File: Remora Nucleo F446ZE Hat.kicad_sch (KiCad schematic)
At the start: 12 parts, among them J1 NucleoF446RE CN10 Header, J11 UART OUT, J17 5V_AUXOUT, J2 NucleoF446RE CN7 Header, J4 5V_SUPPLY

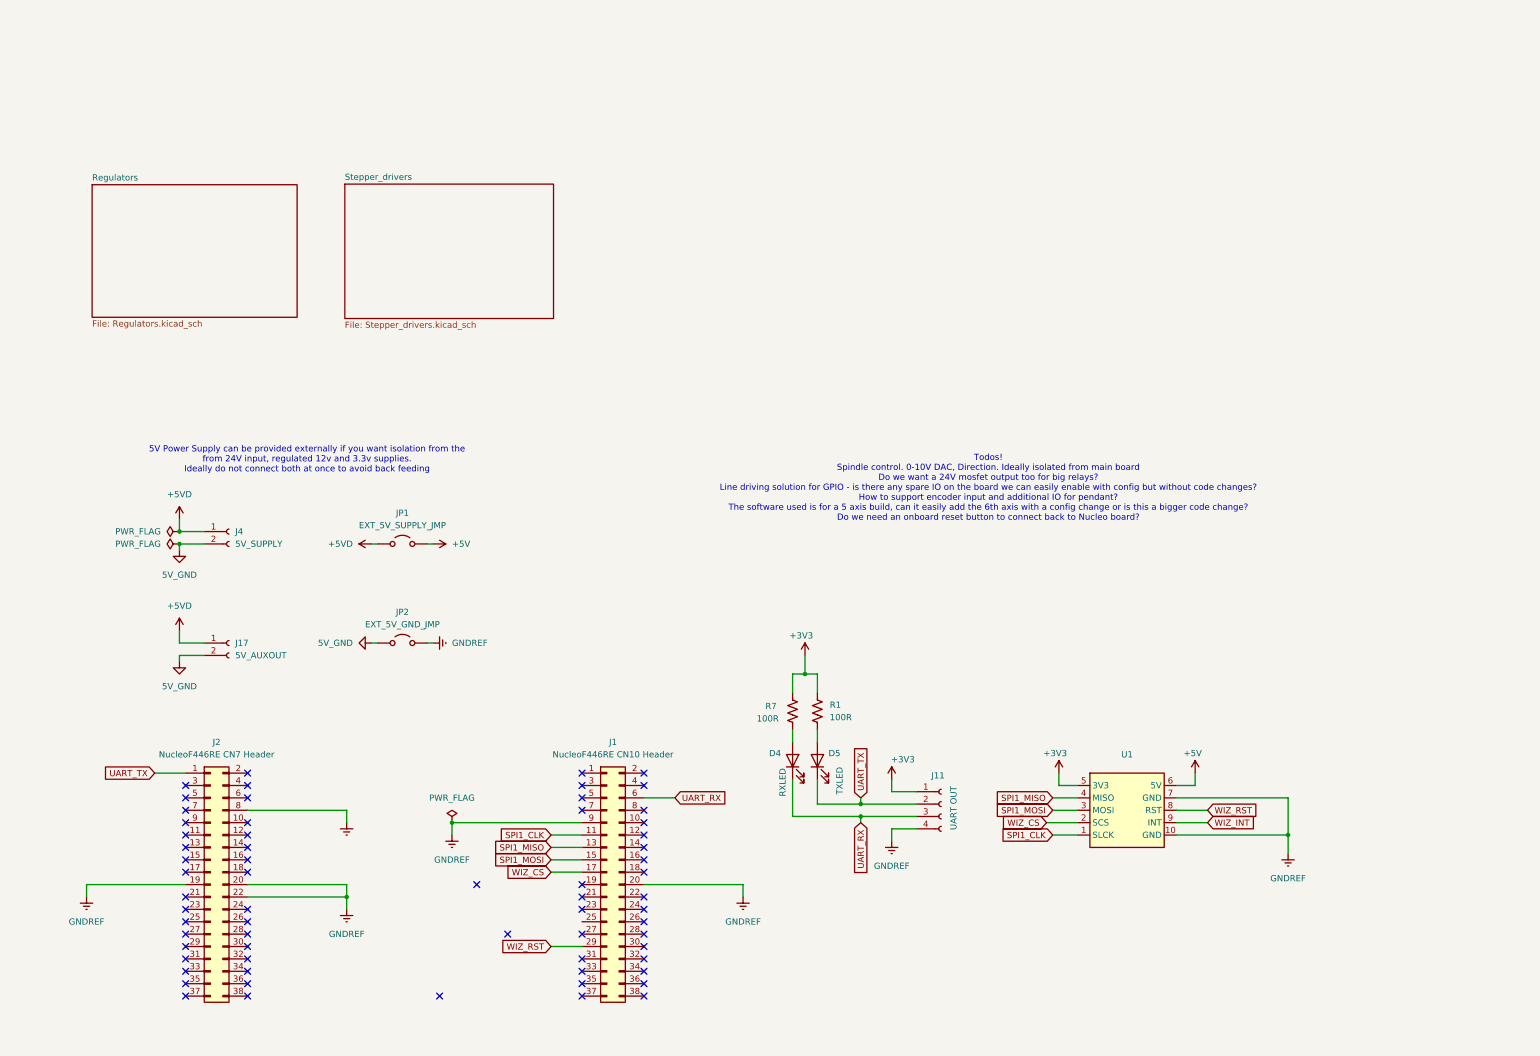
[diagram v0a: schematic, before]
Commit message: Changed board spec from Nucleo F446RE to F446ZE Altered readme to suit it and moved the Todos over.
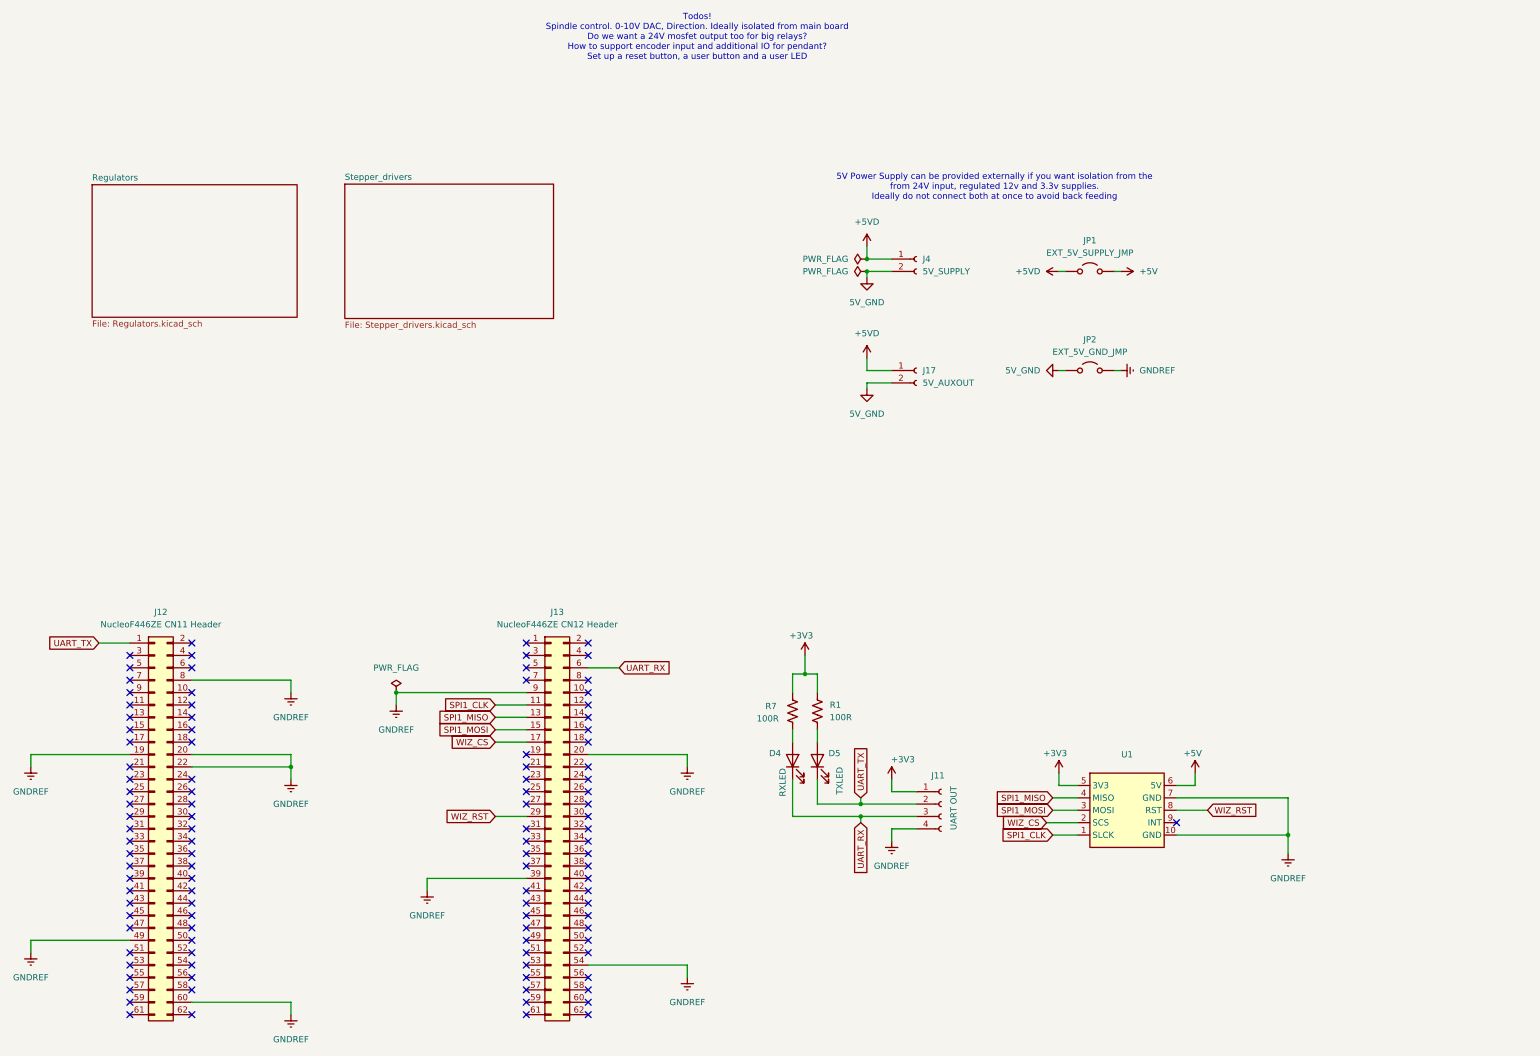
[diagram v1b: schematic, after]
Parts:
- removed J1: NucleoF446RE CN10 Header, Connector_PinHeader_2.54mm:PinHeader_2x19_P2.54mm_Vertical, symbol Connector_Generic:Conn_02x19_Odd_Even
- removed J2: NucleoF446RE CN7 Header, Connector_PinHeader_2.54mm:PinHeader_2x19_P2.54mm_Vertical, symbol Connector_Generic:Conn_02x19_Odd_Even
- added J12: NucleoF446ZE CN11 Header, Connector_PinHeader_2.54mm:PinHeader_2x31_P2.54mm_Vertical, symbol Connector_Generic:Conn_02x31_Odd_Even
- added J13: NucleoF446ZE CN12 Header, Connector_PinHeader_2.54mm:PinHeader_2x31_P2.54mm_Vertical, symbol Connector_Generic:Conn_02x31_Odd_Even
- D4, D5: footprint (none) -> Diode_SMD:D_1206_3216Metric_Pad1.42x1.75mm_HandSolder
- R1, R7: footprint (none) -> Resistor_SMD:R_1206_3216Metric_Pad1.30x1.75mm_HandSolder
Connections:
- net GNDREF: now also J12.19 (Pin_19), J12.20 (Pin_20), J12.22 (Pin_22), J12.49 (Pin_49), J12.60 (Pin_60), J12.8 (Pin_8), J13.20 (Pin_20), J13.39 (Pin_39), J13.54 (Pin_54), J13.9 (Pin_9)
- net SPI1_CLK: now also J13.11 (Pin_11)
- net SPI1_MISO: now also J13.13 (Pin_13)
- net SPI1_MOSI: now also J13.15 (Pin_15)
- net UART_RX: now also J13.6 (Pin_6)
- net UART_TX: now also J12.1 (Pin_1)
- net WIZ_CS: now also J13.17 (Pin_17)
- net WIZ_RST: now also J13.29 (Pin_29)
- net WIZ_INT: no longer names the net of U1.9 (INT)
- no-connect marks 65 -> 108
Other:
- note added: "Todos! Spindle control. 0-10V DAC, Direction. Ideally isolated from main board Do we want a 24V mosfet output too for big relays? How to support encoder input and additional IO for pendant? Set up a reset button, a user button and a user LED"
- note removed: "Todos! Spindle control. 0-10V DAC, Direction. Ideally isolated from main board Do we want a 24V mosfet output too for big relays? Line driving solution for GPIO - is there any spare IO on the board we can easily enable with config but without code changes? How to support encoder input and additional IO for pendant? The software used is for a 5 axis build, can it easily add the 6th axis with a con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"
- moved on the sheet: J17, J4, JP1, JP2

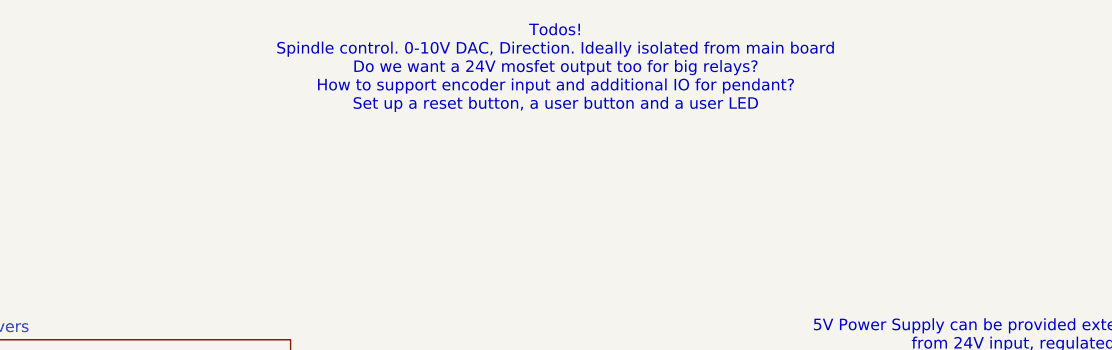
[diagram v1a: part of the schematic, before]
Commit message: tweaked board edge cuts, mouting hole positions and pin headers to match mechanical drawing. Yet to validate with physical hardware
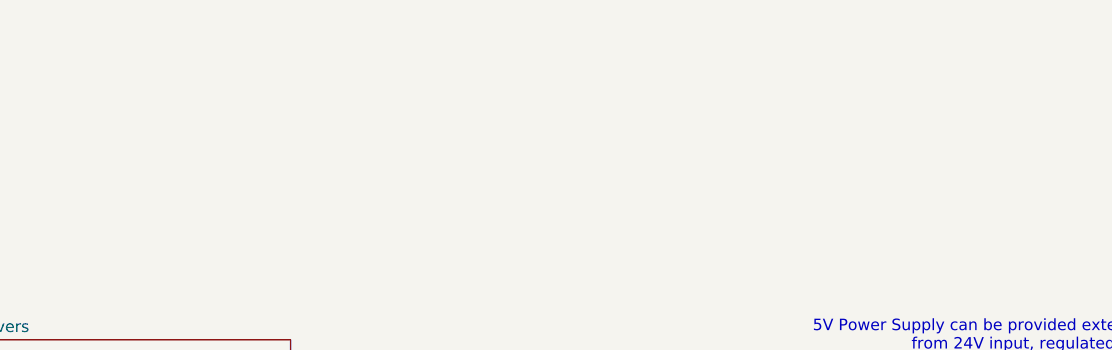
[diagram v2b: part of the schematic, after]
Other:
- note removed: "Todos! Spindle control. 0-10V DAC, Direction. Ideally isolated from main board Do we want a 24V mosfet output too for big relays? How to support encoder input and additional IO for pendant? Set up a reset button, a user button and a user LED"
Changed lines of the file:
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@@
-		)
-	)
-	(text "Todos!\nSpindle control. 0-10V DAC, Direction. Ideally isolated from main board\nDo we want a 24V mosfet output too for big relays?\nHow to support encoder input and additional IO for pendant? \nSet up a reset button, a user button and a user LED"
-		(exclude_from_sim no)
-		(at 154.432 -9.906 0)
-		(effects
-			(font
-				(size 1.27 1.27)
-			)
 		)
 	)

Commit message: rewired the UART to use virtual comm port
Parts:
- removed D4: RXLED, Diode_SMD:D_1206_3216Metric_Pad1.42x1.75mm_HandSolder, symbol Device:LED
- removed J11: UART OUT, symbol Connector:Conn_01x04_Socket
- removed R7: 100R, Resistor_SMD:R_1206_3216Metric_Pad1.30x1.75mm_HandSolder, symbol Device:R_US
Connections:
- net UART_TX: now also J13.10 (Pin_10); no longer J12.1 (Pin_1)
- net UART_RX: no longer names the net of J13.6 (Pin_6)
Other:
- moved on the sheet: D5, R1

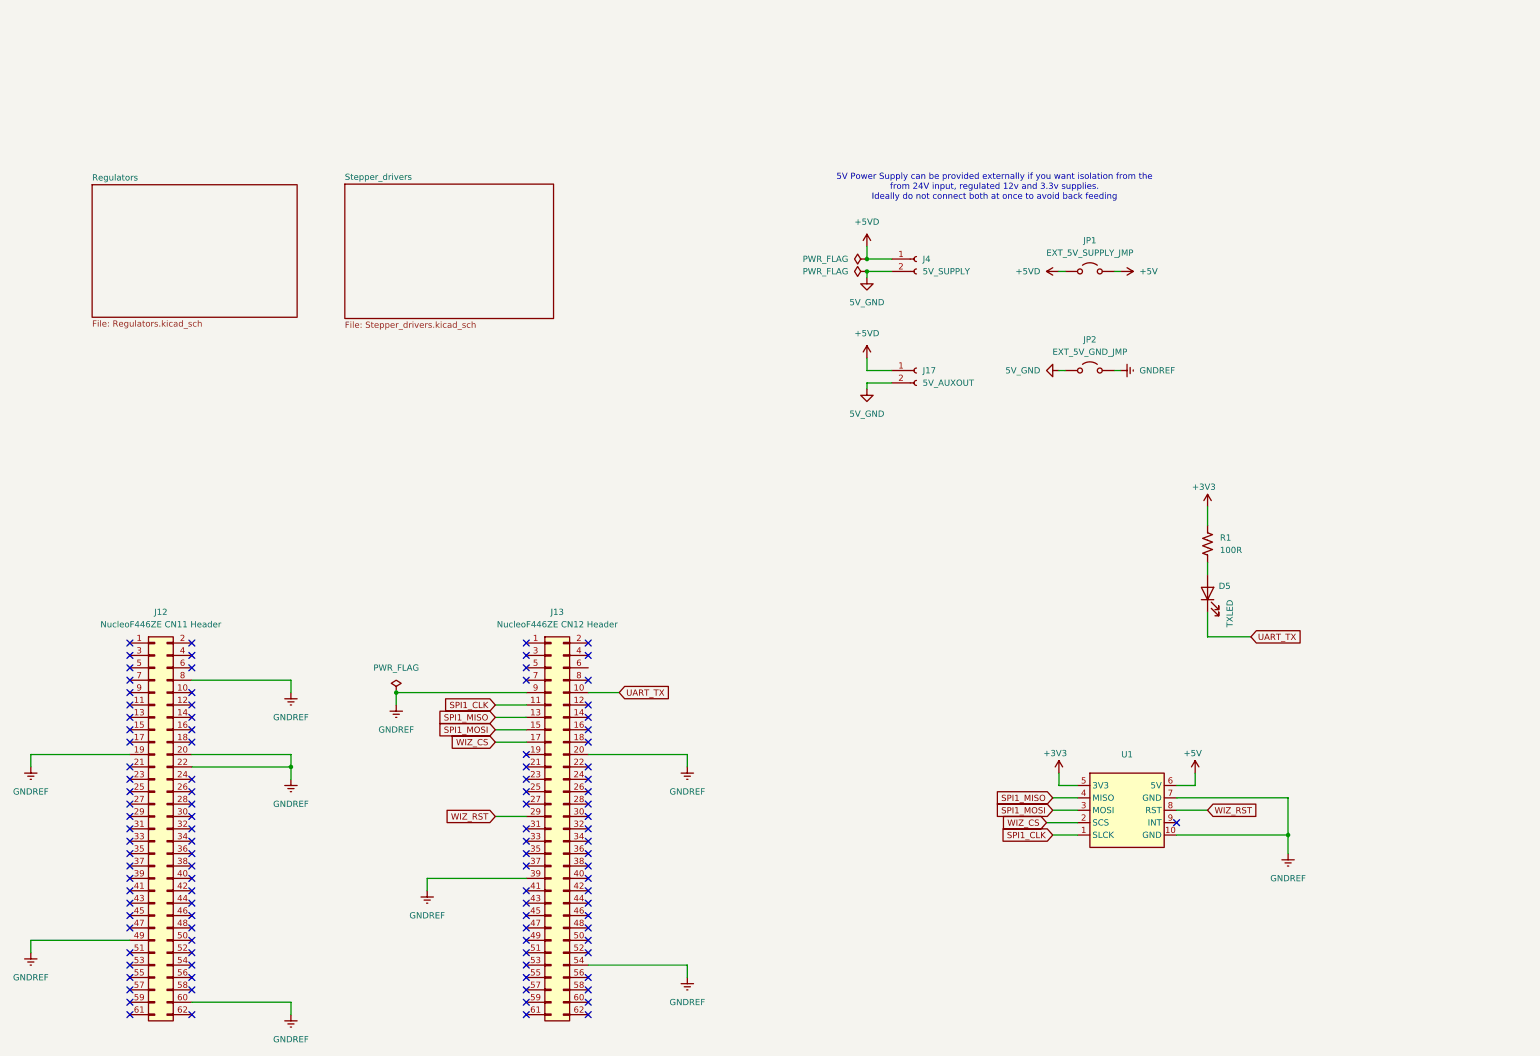
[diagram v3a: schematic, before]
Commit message: changes some unecessary global labels to local. Added a heirarchical sheet for output driver and basic numbering. Sink logic not yet set for O/Ps, but placeholder for now
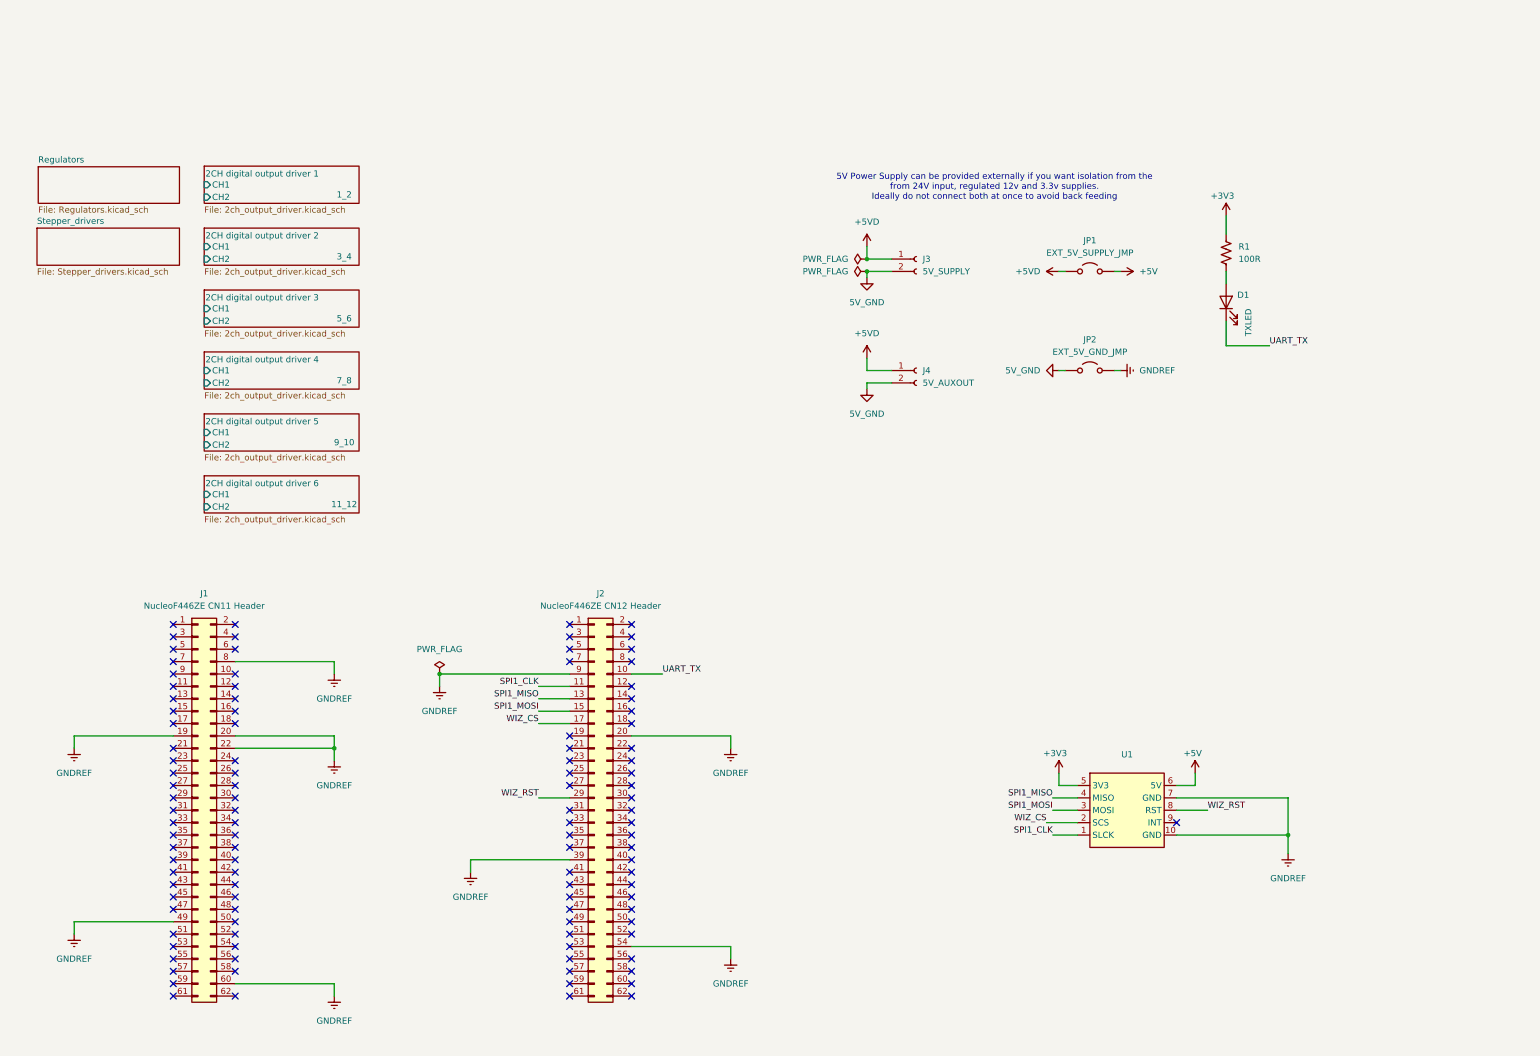
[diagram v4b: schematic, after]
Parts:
- renumbered D5 to D1, J12 to J1, J13 to J2, J4 to J3, J17 to J4
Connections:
- no-connect marks 108 -> 109
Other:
- added sheet 2CH digital output driver 1 (2ch_output_driver.kicad_sch)
- added sheet 2CH digital output driver 2 (2ch_output_driver.kicad_sch)
- added sheet 2CH digital output driver 3 (2ch_output_driver.kicad_sch)
- added sheet 2CH digital output driver 4 (2ch_output_driver.kicad_sch)
- added sheet 2CH digital output driver 5 (2ch_output_driver.kicad_sch)
- added sheet 2CH digital output driver 6 (2ch_output_driver.kicad_sch)
- moved on the sheet: D1, J1, J2, R1
